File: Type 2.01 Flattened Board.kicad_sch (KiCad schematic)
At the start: 8 parts, among them U10 74AHC125

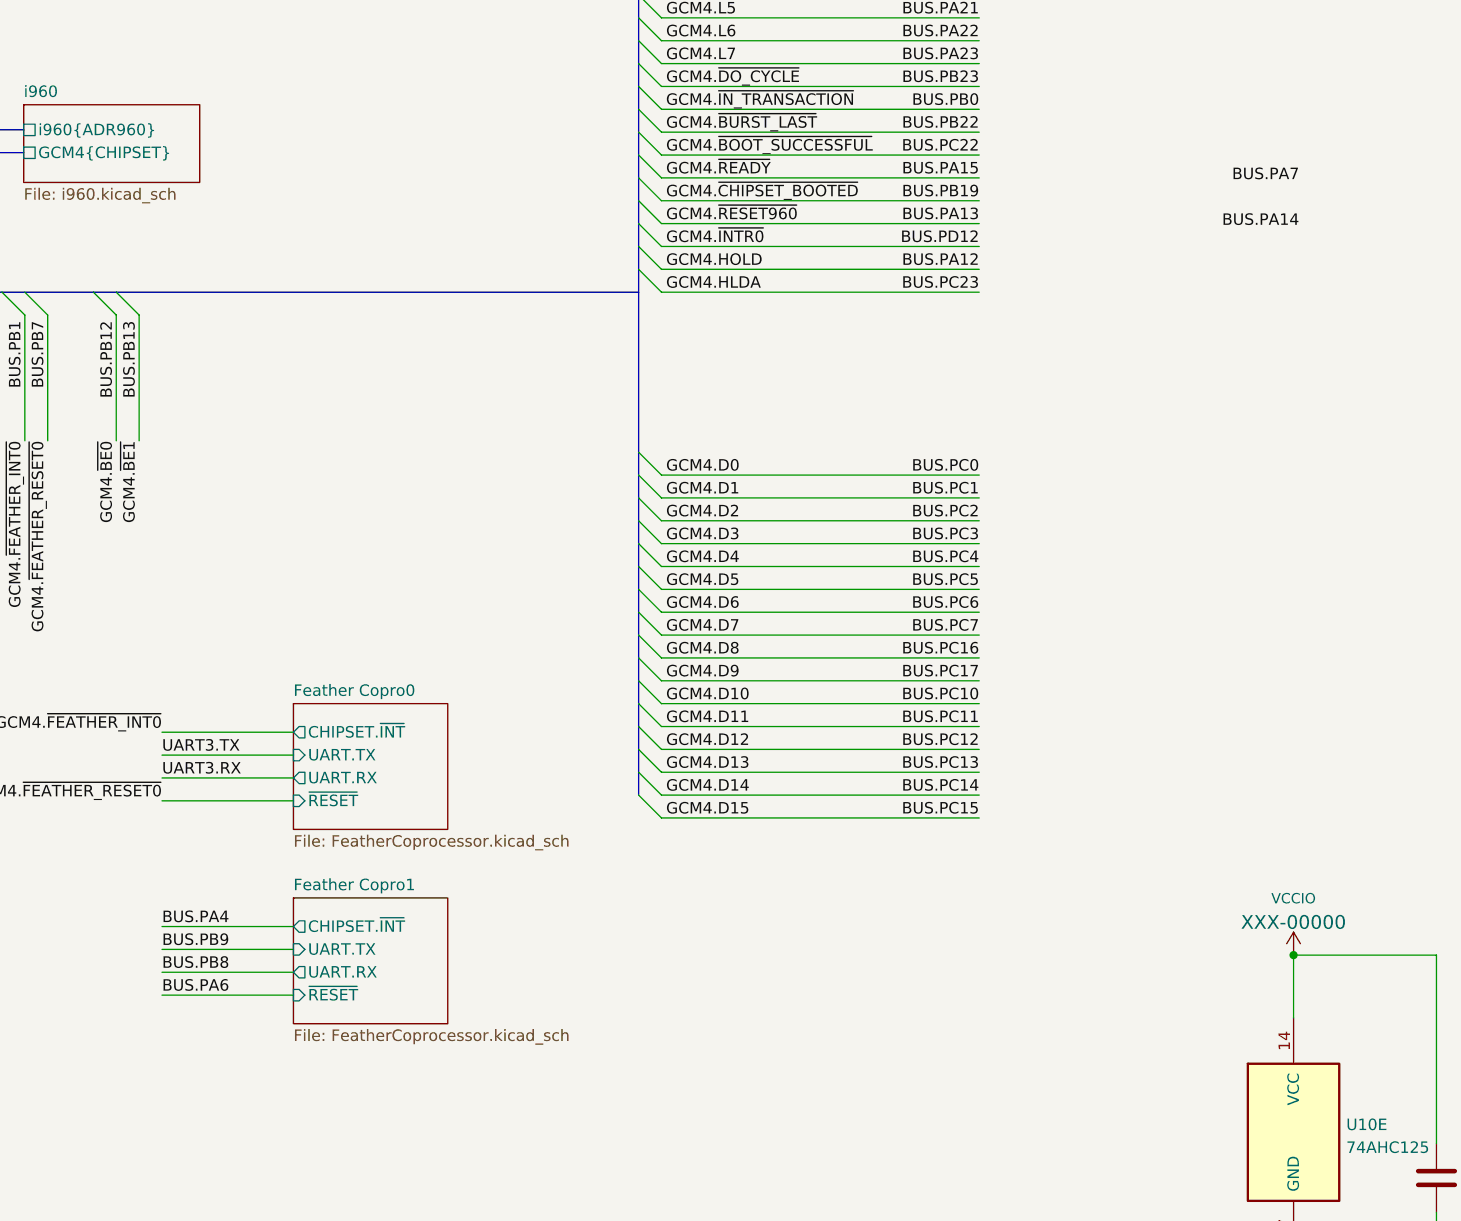
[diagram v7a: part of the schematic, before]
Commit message: Added feather wing sockets next to each plug
F1 has its battery connector blocked by the dazzler shield.

This is not that big of a deal to be honest.
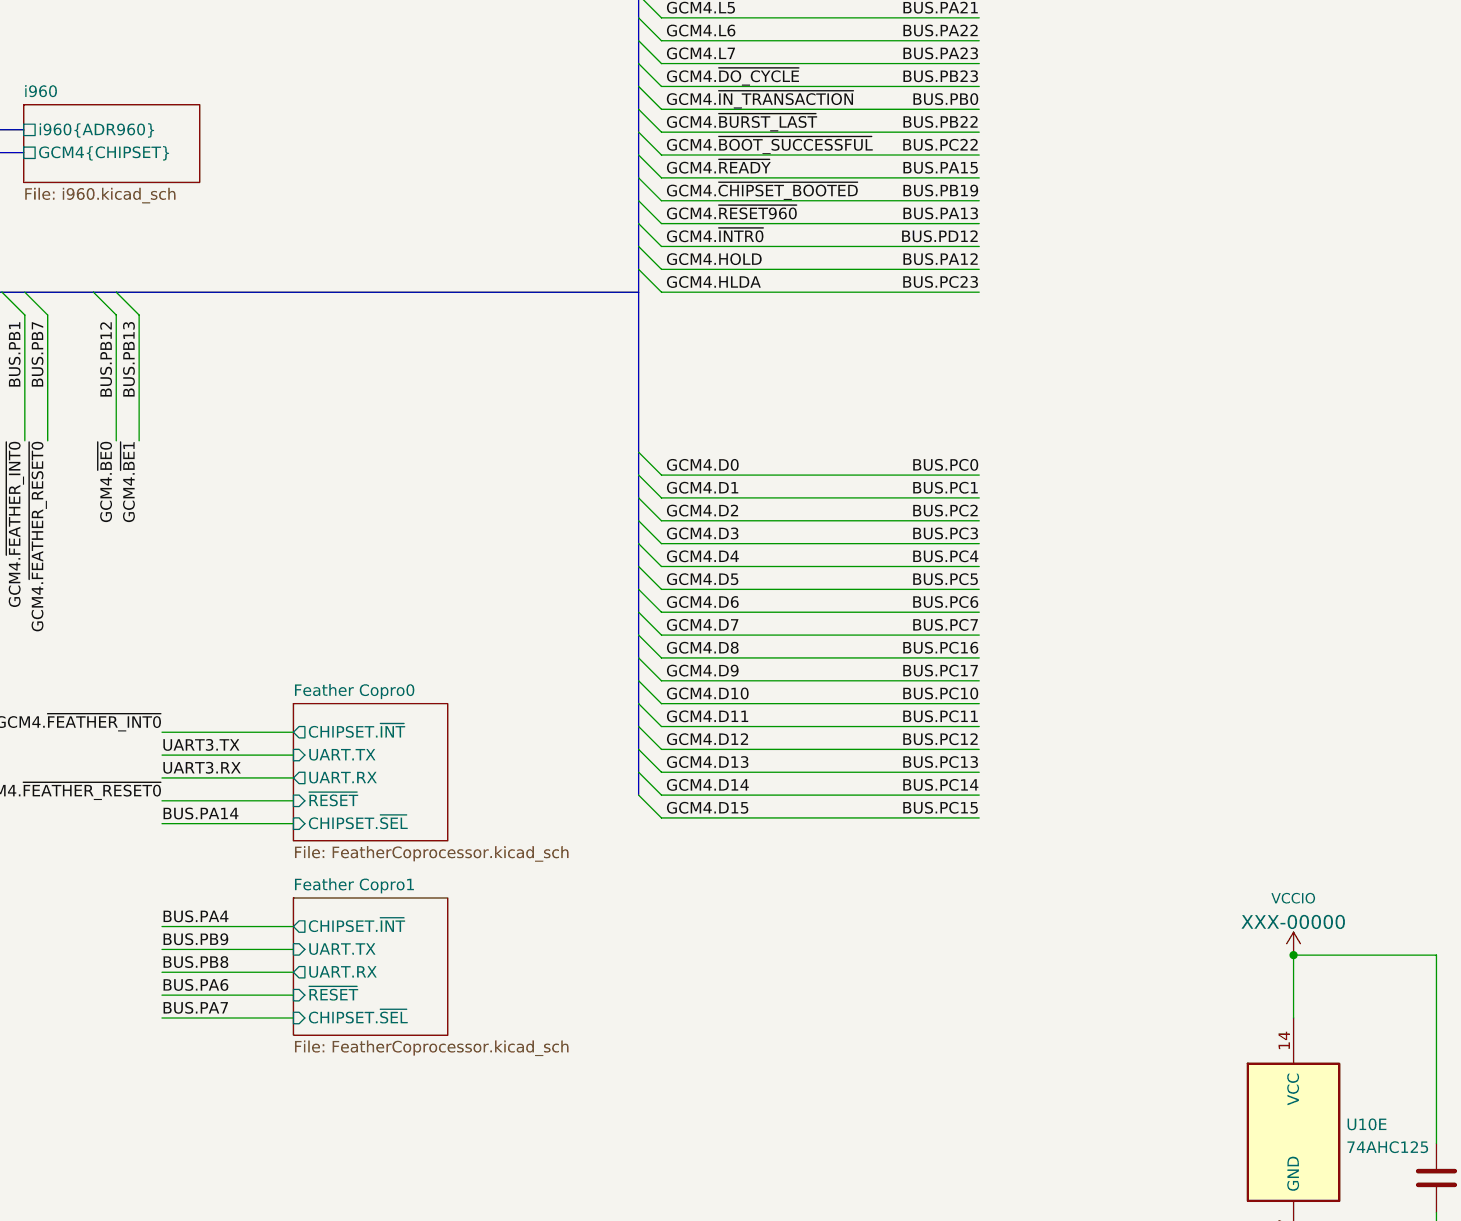
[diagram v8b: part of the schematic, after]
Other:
- sheet Feather Copro0 ports: added CHIPSET.~{SEL}; removed none
- sheet Feather Copro1 ports: added CHIPSET.~{SEL}; removed none
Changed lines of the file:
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@@
+    (stroke (width 0) (type default) (color 0 0 0 0))
+  )
+  (wire (pts (xy 256.54 167.005) (xy 271.145 167.005))
     (stroke (width 0) (type default) (color 0 0 0 0))
   )
@@
   )
   (bus (pts (xy 189.992 149.352) (xy 189.992 151.892))
+    (stroke (width 0) (type default) (color 0 0 0 0))
+  )
+  (wire (pts (xy 256.54 145.415) (xy 271.145 145.415))
     (stroke (width 0) (type default) (color 0 0 0 0))
   )
@@
     (effects (font (size 1.27 1.27)) (justify left bottom))
   )
-  (label "BUS.PA14" (at 382.905 79.375 180)
-    (effects (font (size 1.27 1.27)) (justify right bottom))
+  (label "BUS.PA14" (at 256.54 145.415 0)
+    (effects (font (size 1.27 1.27)) (justify left bottom))
   )
   (label "BUS.PA17" (at 347.345 45.72 180)
@@
     (effects (font (size 1.27 1.27)) (justify left bottom))
   )
-  (label "BUS.PA7" (at 382.905 74.295 180)
-    (effects (font (size 1.27 1.27)) (justify right bottom))
+  (label "BUS.PA7" (at 256.54 167.005 0)
+    (effects (font (size 1.27 1.27)) (justify left bottom))
   )
   (label "BUS.PD12" (at 347.345 81.28 180)
@@
     (pin "7")
   )
-  (sheet (at 271.145 153.67) (size 17.145 13.97) (fields_autoplaced)
+  (sheet (at 271.145 153.67) (size 17.145 15.24) (fields_autoplaced)
     (stroke (width 0.1524) (type solid) (color 0 0 0 0))
     (fill (color 0 0 0 0.0000))
@@
       (effects (font (size 1.27 1.27)) (justify left bottom))
     )
-    (property "Sheet file" "FeatherCoprocessor.kicad_sch" (id 1) (at 271.145 168.2246 0)
+    (property "Sheet file" "FeatherCoprocessor.kicad_sch" (id 1) (at 271.145 169.4946 0)
       (effects (font (size 1.27 1.27)) (justify left top))
     )
@@
     )
     (pin "~{RESET}" input (at 271.145 164.465 180)
+      (effects (font (size 1.27 1.27)) (justify left))
+    )
+    (pin "CHIPSET.~{SEL}" input (at 271.145 167.005 180)
       (effects (font (size 1.27 1.27)) (justify left))
     )
@@
     )
   )
-  (sheet (at 271.145 132.08) (size 17.145 13.97) (fields_autoplaced)
+  (sheet (at 271.145 132.08) (size 17.145 15.24) (fields_autoplaced)
     (stroke (width 0.1524) (type solid) (color 0 0 0 0))
     (fill (color 0 0 0 0.0000))
@@
       (effects (font (size 1.27 1.27)) (justify left bottom))
     )
-    (property "Sheet file" "FeatherCoprocessor.kicad_sch" (id 1) (at 271.145 146.6346 0)
+    (property "Sheet file" "FeatherCoprocessor.kicad_sch" (id 1) (at 271.145 147.9046 0)
       (effects (font (size 1.27 1.27)) (justify left top))
     )
@@
     )
     (pin "~{RESET}" input (at 271.145 142.875 180)
+      (effects (font (size 1.27 1.27)) (justify left))
+    )
+    (pin "CHIPSET.~{SEL}" input (at 271.145 145.415 180)
       (effects (font (size 1.27 1.27)) (justify left))
     )
@@
       (reference "#PWR06") (unit 1) (value "+5V") (footprint "")
     )
+    (path "/33147676-43f8-493a-9a6a-8cf437a2c6b4/301e903c-c1b0-4eaf-9dfc-ced02cd4b875"
+      (reference "#PWR07") (unit 1) (value "+3.3V") (footprint "")
+    )
+    (path "/33147676-43f8-493a-9a6a-8cf437a2c6b4/9a697ca2-426b-4221-a3a0-a2991f47de8b"
+      (reference "#PWR08") (unit 1) (value "GND") (footprint "")
+    )
     (path "/cd4173d7-5549-43d9-b4b1-83989500a84c/a626156e-d4b9-4c78-b816-3dc9dcecdaf5"
       (reference "#PWR09") (unit 1) (value "+5V") (footprint "")
@@
       (reference "#PWR010") (unit 1) (value "GND") (footprint "")
     )
+    (path "/33147676-43f8-493a-9a6a-8cf437a2c6b4/456c2675-8038-46e2-9d89-8539dc3f242c"
+      (reference "#PWR011") (unit 1) (value "+3.3V") (footprint "")
+    )
+    (path "/33147676-43f8-493a-9a6a-8cf437a2c6b4/4dc9d2e9-7762-46d8-b41d-17a3cf9fb6cb"
+      (reference "#PWR012") (unit 1) (value "+5V") (footprint "")
+    )
     (path "/666eaa1f-94aa-46e3-a7dc-28dfe7618aa9"
       (reference "#PWR013") (unit 1) (value "GND") (footprint "")
     )
+    (path "/c9365d17-b900-4bd3-b96d-5359e9255bd9/301e903c-c1b0-4eaf-9dfc-ced02cd4b875"
+      (reference "#PWR014") (unit 1) (value "+3.3V") (footprint "")
+    )
+    (path "/c9365d17-b900-4bd3-b96d-5359e9255bd9/9a697ca2-426b-4221-a3a0-a2991f47de8b"
+      (reference "#PWR015") (unit 1) (value "GND") (footprint "")
+    )
+    (path "/c9365d17-b900-4bd3-b96d-5359e9255bd9/456c2675-8038-46e2-9d89-8539dc3f242c"
+      (reference "#PWR016") (unit 1) (value "+3.3V") (footprint "")
+    )
     (path "/bceabf0e-2710-4ae7-8c4a-c9f97abb3b18"
       (reference "#PWR017") (unit 1) (value "GND") (footprint "")
     )
+    (path "/c9365d17-b900-4bd3-b96d-5359e9255bd9/4dc9d2e9-7762-46d8-b41d-17a3cf9fb6cb"
+      (reference "#PWR018") (unit 1) (value "+5V") (footprint "")
+    )
     (path "/3ad50359-adcb-45da-a8b2-e582d67a0fe4"
       (reference "#PWR019") (unit 1) (value "GND") (footprint "")
@@
       (reference "U12") (unit 1) (value "74AHC245") (footprint "Package_DIP:DIP-20_W7.62mm_Socket")
     )
+    (path "/33147676-43f8-493a-9a6a-8cf437a2c6b4/decd8d65-b8d6-46e0-86ad-86a60c20c42e"
+      (reference "U13") (unit 1) (value "Adafruit_FeatherWing") (footprint "Module:Adafruit_Feather")
+    )
     (path "/cd4173d7-5549-43d9-b4b1-83989500a84c/f1699c43-cf0a-4255-89c0-107adf651abd"
       (reference "U14") (unit 1) (value "GAL16V8") (footprint "Package_DIP:DIP-20_W7.62mm_Socket")
@@
       (reference "U18") (unit 1) (value "74AHC573") (footprint "Package_DIP:DIP-20_W7.62mm_Socket")
     )
+    (path "/c9365d17-b900-4bd3-b96d-5359e9255bd9/decd8d65-b8d6-46e0-86ad-86a60c20c42e"
+      (reference "U19") (unit 1) (value "Adafruit_FeatherWing") (footprint "Module:Adafruit_Feather")
+    )
     (path "/2bd6b25f-a519-4224-8dd9-2e42d262ce2e"
